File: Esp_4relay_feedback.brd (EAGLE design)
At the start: 100 x 100 mm, 58 parts, among them IC1 LM1117MP-3.3, IC2 7805TV, IC3 7805TV, IC4 7805TV, K1 G5LE, K2 G5LE, K3 G5LE, K4 G5LE, Q1 16MHz, SW1 Push Switch, T1 BC547, T2 BC547, T3 BC547, T4 BC547, U2 ATMEGA328P_PDIP

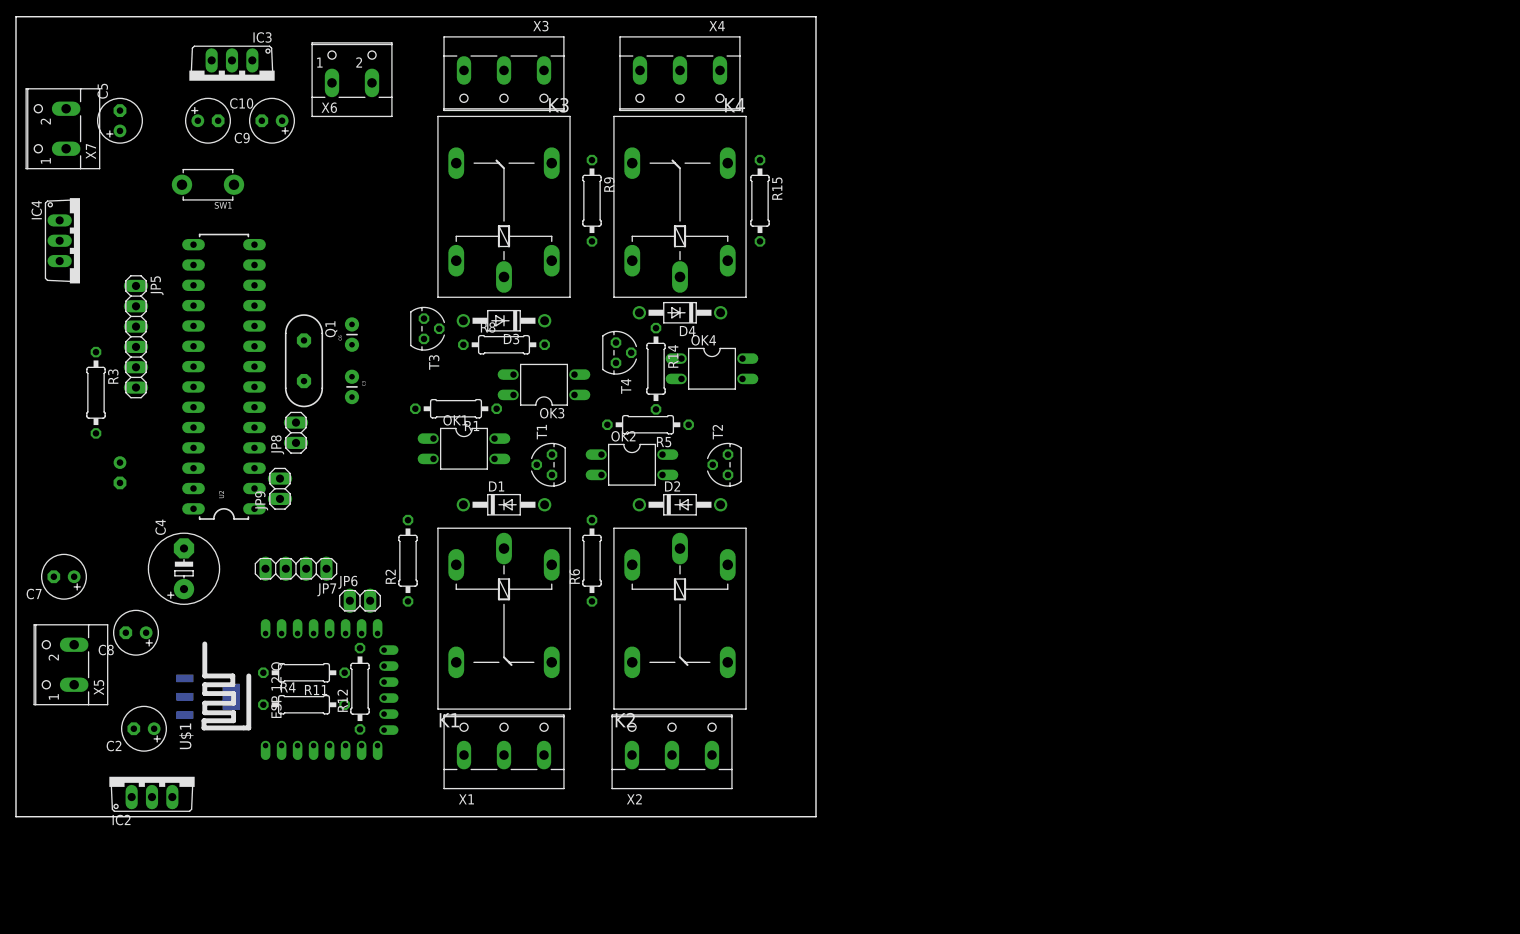
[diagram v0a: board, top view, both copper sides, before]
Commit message: added 8 relays
8 relays arranged in 4 up-down manner with
esp and atmega328 at left side.

routing 70% completed.
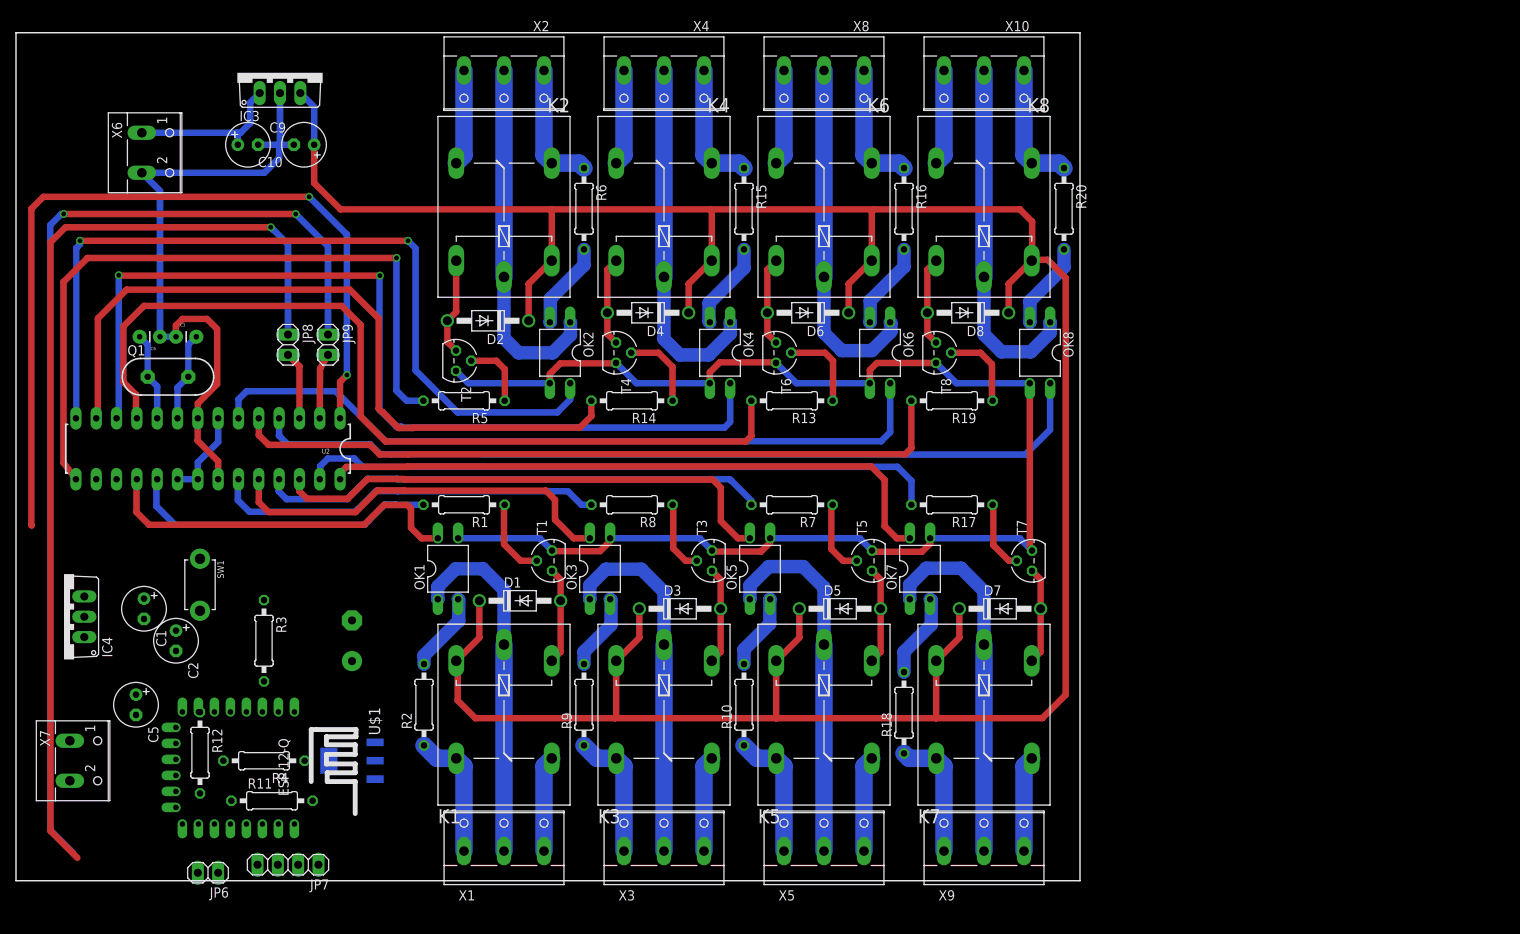
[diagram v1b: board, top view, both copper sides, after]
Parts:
- removed C7, C8: 10uf, rcl:E2,5-6
- removed IC2: 7805TV, linear:TO220V
- removed JP5: (no value), pinhead:1X06
- added D5, D6, D7, D8: 1N4007, diode:DO41-10
- added K5, K6, K7, K8: G5LE, relay:G5LE
- added OK5, OK6, OK7, OK8: PC817, optocoupler:DIL04
- added R10, R16, R18, R20: 220k, rcl:0207/10
- added R13, R17, R19, R7: 1k, rcl:0207/10
- added T5, T6, T7, T8: BC547, transistor:TO92
- added X10, X8, X9: (no value), con-wago-500:W237-103
- X5: device con-wago-500:W237-102 -> con-wago-500:W237-103
- moved X5 97.5 mm to (161.0, -3.00), turned to 0 degrees
- moved X3 97.1 mm to (141.0, -3.00), turned to 0 degrees
- moved X2 85.6 mm to (121.0, 92.0), turned to 180 degrees
- moved X7 79.1 mm to (68.0, 7.00), turned to 270 degrees
- moved C5 73.0 mm to (75.0, 14.0), turned to 270 degrees
- moved K3 68.0 mm to (141.0, 12.0), turned to 270 degrees
- moved R9 63.0 mm to (131.0, 14.0), turned to 90 degrees
- moved K2 57.4 mm to (121.0, 77.0), turned to 90 degrees
- moved SW1 50.0 mm to (83.0, 29.0), turned to 270 degrees
- moved IC4 47.0 mm to (66.0, 25.0), turned to 90 degrees
- moved T3 46.2 mm to (147.0, 32.0), turned to 90 degrees
- moved R6 44.0 mm to (131.0, 76.0), turned to 270 degrees
- moved D3 42.2 mm to (143.0, 26.0), turned to 0 degrees
- moved JP6 38.9 mm to (84.0, -7.00), turned to 180 degrees
- moved R3 37.4 mm to (91.0, 22.0)
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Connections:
- removed net ESP_SUPPLY: C2.+, C8.+, IC1.3, IC2.3
- new net F5: OK5.4, U2.26
- new net F6: OK6.4, U2.6
- new net F7: OK7.4, U2.28
- new net F8: OK8.4, U2.4
- new net N$34: OK5.2, R10.2
- new net N$35: R7.1, T5.2
- new net N$46: D5.A, K5.2, T5.3
- new net N$47: K6.P, OK6.1, X8.2
- new net N$48: K6.S, R16.1, X8.1
- new net N$49: OK6.2, R16.2
- new net N$50: R13.1, T6.2
- new net N$51: D6.A, K6.2, T6.3
- new net N$52: K7.P, OK7.1, X9.2
- new net N$53: K7.S, R18.1, X9.1
- new net N$54: OK7.2, R18.2
- new net N$55: R17.1, T7.2
- new net N$56: D7.A, K7.2, T7.3
- new net N$57: K8.P, OK8.1, X10.2
- new net N$58: K8.S, R20.1, X10.1
- new net N$59: OK8.2, R20.2
- new net N$60: R19.1, T8.2
- new net N$61: D8.A, K8.2, T8.3
- new net N$62: K5.O, X5.3
- new net N$63: K6.O, X8.3
- new net N$64: K7.O, X9.3
- new net N$65: K8.O, X10.3
- new net R5: R7.2, U2.25
- new net R6: R13.2, U2.11
- new net R7: R17.2, U2.27
- new net R8: R19.2, U2.5
- net F1: now also U2.18; no longer U2.5
- net F2: now also U2.14; no longer U2.11
- net F3: now also U2.24; no longer U2.13
- net F4: now also U2.12; no longer U2.15
- net GND: now also OK5.3, OK6.3, OK7.3, OK8.3, T5.1, T6.1, T7.1, T8.1; no longer C7.-, C8.-, IC2.2, JP5.6, X5.2
- net N$16: now also K5.P, OK5.1, X5.2; no longer JP5.3, U2.19
- net N$23: now also U2.16; no longer JP5.2, U2.18
- net N$26: now also U2.17; no longer C7.+, IC2.1, X5.1
- net N$32: now also K5.S, R10.1, X5.1; no longer JP5.1, U2.17
- net R1: now also U2.19; no longer U2.4
- net R2: now also U2.15; no longer U2.6
- net R3: now also U2.23; no longer U2.12
- net R4: now also U2.13; no longer U2.14
- net RELAY_SUPPLY: now also D5.C, D6.C, D7.C, D8.C, K5.1, K6.1, K7.1, K8.1
- net RESET: no longer JP5.4
- net VCC: now also C2.+, IC1.3; no longer JP5.5
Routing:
- net RELAY_SUPPLY: track 0.00 -> 353.8 mm
- net GND: track 0.00 -> 262.0 mm
- net TX1: track 0.00 -> 127.7 mm, vias 0 -> 2
- net RX1: track 0.00 -> 121.0 mm, vias 0 -> 1
- net F4: track 0.00 -> 117.3 mm, vias 0 -> 2
- net R6: track 0.00 -> 110.1 mm
- net F8: track 0.00 -> 106.7 mm
- net RESET: track 0.00 -> 105.0 mm, vias 0 -> 2
- net F2: track 0.00 -> 104.2 mm, vias 0 -> 2
- net F6: track 0.00 -> 93.4 mm
- net R4: track 0.00 -> 92.0 mm
- net R8: track 0.00 -> 90.9 mm
- net R2: track 0.00 -> 88.5 mm, vias 0 -> 1
- net R7: track 0.00 -> 80.1 mm
- net F7: track 0.00 -> 79.4 mm
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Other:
- board size 100 x 100 mm -> 133 x 106 mm

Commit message: routing done
board routing completed 100%
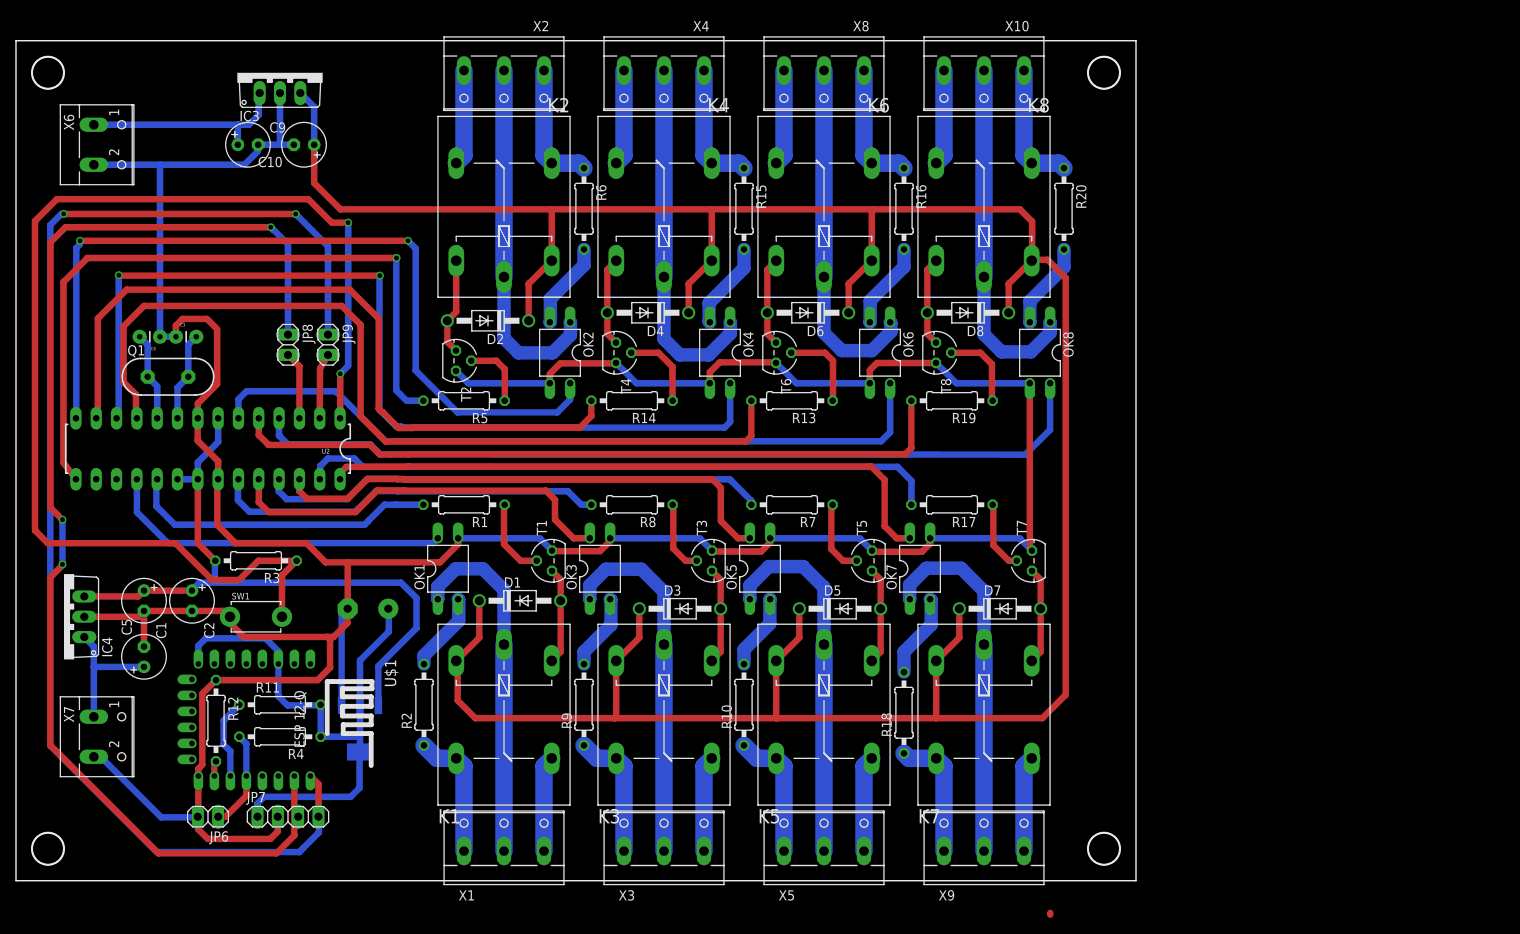
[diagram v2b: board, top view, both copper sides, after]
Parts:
- moved R11 12.0 mm to (93.0, 14.0)
- moved R3 10.0 mm to (90.0, 32.0), turned to 180 degrees
- moved SW1 8.06 mm to (90.0, 25.0), turned to 0 degrees
- moved JP6 7.00 mm to (84.0, 0.00)
- moved U$1 6.32 mm to (91.0, 12.0)
- moved C5 6.08 mm to (76.0, 20.0), turned to 90 degrees
- moved X6 6.08 mm to (71.0, 84.0)
- moved JP7 6.00 mm to (94.0, 0.00), turned to 0 degrees
- moved C2 5.39 mm to (82.0, 27.0)
- moved C4 4.47 mm to (104.0, 26.0), turned to 0 degrees
- moved R12 4.47 mm to (85.0, 12.0)
- moved X7 4.24 mm to (71.0, 10.0)
- moved IC1 4.12 mm to (103.0, 11.0), turned to 180 degrees
- moved R4 3.61 mm to (93.0, 10.0)
- moved C1 1.00 mm to (76.0, 27.0)
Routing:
- net GND: track 262.0 -> 431.3 mm
- net 3V3: track 0.00 -> 72.9 mm
- net VCC: track 11.2 -> 83.6 mm
- net RESET: track 105.0 -> 149.1 mm
- net TX1: track 127.7 -> 160.7 mm
- net RX1: track 121.0 -> 151.9 mm, vias 1 -> 3
- net N$33: track 0.00 -> 16.7 mm
- net IO0: track 0.00 -> 12.4 mm
- net N$21: track 0.00 -> 10.1 mm
- net N$27: track 19.8 -> 26.4 mm
- net F1: track 46.6 -> 43.6 mm
- net IO15: track 0.00 -> 1.90 mm
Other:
- board size 133 x 106 mm -> 140 x 105 mm

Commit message: component placing changed
Controller and esp placed in between relays.
routing done
PCB size : 130X95mm
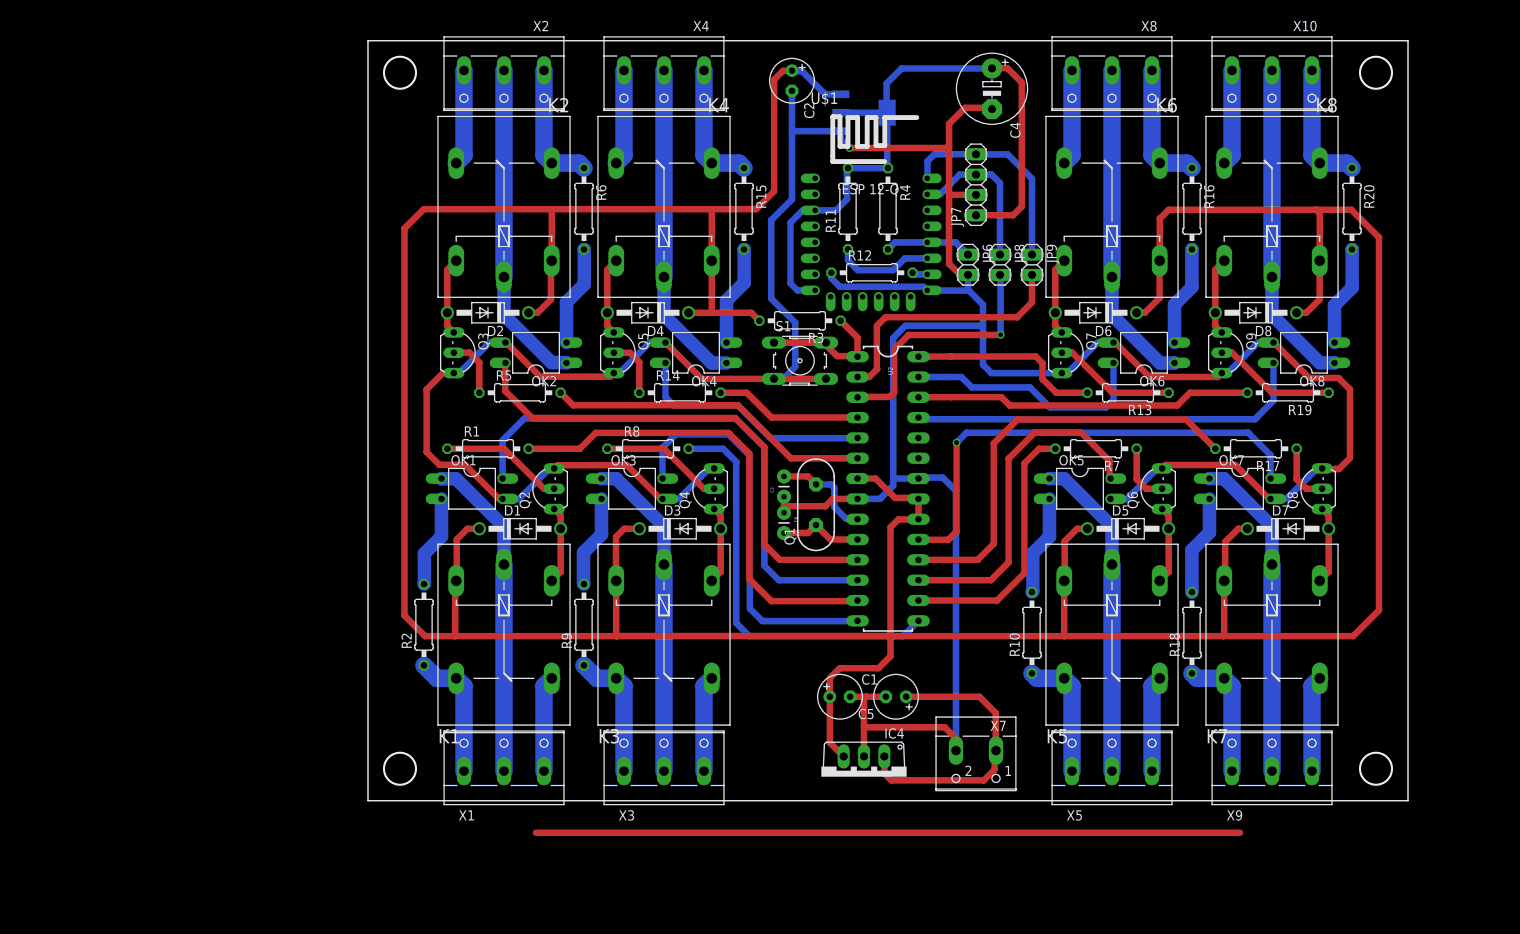
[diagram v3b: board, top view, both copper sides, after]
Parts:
- removed C10, C9: 10uf, rcl:E2,5-6
- removed IC3: 7805TV, linear:TO220V
- removed SW1: Push Switch, adafruit:TACT_PANA-EVQ
- removed T1, T2, T3, T4, T5, T6, T7, T8: BC547, transistor:TO92
- removed X6: (no value), con-wago-500:W237-102
- added Q2, Q3, Q4, Q5, Q6, Q7, Q8, Q9: BC547, transistor-npn:TO92-EBC
- added S1: (no value), switch-omron:B3F-10XX
- moved JP6 117.4 mm to (179.0, 69.0), turned to 270 degrees
- moved JP7 116.8 mm to (180.0, 79.0), turned to 90 degrees
- moved X7 109.0 mm to (180.0, 7.00), turned to 180 degrees
- moved IC4 102.0 mm to (166.0, 5.00), turned to 180 degrees
- moved C4 101.5 mm to (182.0, 91.0), flipped to the top, turned to 270 degrees
- moved R4 100.7 mm to (169.0, 76.0), turned to 270 degrees
- moved IC1 99.5 mm to (166.0, 88.0), turned to 90 degrees
- moved R12 99.3 mm to (167.0, 68.0), turned to 0 degrees
- moved C2 99.2 mm to (157.0, 92.0)
- moved U$1 98.1 mm to (167.0, 74.0), turned to 0 degrees
- moved R11 94.3 mm to (164.0, 76.0), turned to 90 degrees
- moved C5 94.1 mm to (170.0, 15.0), turned to 180 degrees
- moved JP8 89.6 mm to (183.0, 69.0)
- moved JP9 88.6 mm to (187.0, 69.0)
- moved C1 87.8 mm to (163.0, 15.0), turned to 0 degrees
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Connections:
- removed net N$23: U2.16
- removed net N$26: U2.17
- removed net N$27: C9.+, IC3.1, X6.1
- removed net RELAY_SUPPLY: C10.+, D1.C, D2.C, D3.C, D4.C, D5.C, D6.C, D7.C, D8.C, IC3.3, K1.1, K2.1, K3.1, K4.1, K5.1, K6.1, K7.1, K8.1
- new net ERT: U2.23
- new net WE: U2.24
- net F1: now also U2.12; no longer U2.18
- net F2: now also U2.11; no longer U2.14
- net F3: now also U2.14; no longer U2.24
- net F4: now also U2.5; no longer U2.12
- net F5: now also U2.17; no longer U2.26
- net F6: now also U2.27; no longer U2.6
- net F7: now also U2.19; no longer U2.28
- net F8: now also U2.25; no longer U2.4
- net GND: now also Q2.E, Q3.E, Q4.E, Q5.E, Q6.E, Q7.E, Q8.E, Q9.E, S1.3, S1.4; no longer C10.-, C9.-, IC3.2, SW1.P$1, T1.1, T2.1, T3.1, T4.1, T5.1, T6.1, T7.1, T8.1, X6.2
- net N$11: now also Q3.B; no longer T2.2
- net N$12: now also Q3.C; no longer T2.3
- net N$17: now also Q4.B; no longer T3.2
- net N$18: now also Q4.C; no longer T3.3
- net N$24: now also Q5.B; no longer T4.2
- net N$25: now also Q5.C; no longer T4.3
- net N$35: now also Q6.B; no longer T5.2
- net N$46: now also Q6.C; no longer T5.3
- net N$50: now also Q7.B; no longer T6.2
- net N$51: now also Q7.C; no longer T6.3
- net N$55: now also Q8.B; no longer T7.2
- net N$56: now also Q8.C; no longer T7.3
- net N$60: now also Q9.B; no longer T8.2
- net N$61: now also Q9.C; no longer T8.3
- net N$7: now also Q2.B; no longer T1.2
- net N$8: now also Q2.C; no longer T1.3
- net R1: now also U2.13; no longer U2.19
- net R2: now also U2.6; no longer U2.15
- net R3: now also U2.15; no longer U2.23
- net R4: now also U2.4; no longer U2.13
- net R5: now also U2.16; no longer U2.25
- net R6: now also U2.28; no longer U2.11
- net R7: now also U2.18; no longer U2.27
- net R8: now also U2.26; no longer U2.5
- net RESET: now also S1.1, S1.2; no longer SW1.P$2
- net VCC: now also D1.C, D2.C, D3.C, D4.C, D5.C, D6.C, D7.C, D8.C, K1.1, K2.1, K3.1, K4.1, K5.1, K6.1, K7.1, K8.1
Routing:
- net VCC: track 83.6 -> 499.1 mm
- net RELAY_SUPPLY: track 353.8 -> 0.00 mm
- net TX1: track 160.7 -> 26.3 mm, vias 2 -> 0
- net RX1: track 151.9 -> 19.5 mm, vias 3 -> 0
- net RESET: track 149.1 -> 16.7 mm, vias 2 -> 0
- net N$23: track 0.00 -> 88.0 mm
- net F4: track 117.3 -> 30.4 mm, vias 2 -> 0
- net R6: track 110.1 -> 24.1 mm
- net R4: track 92.0 -> 18.4 mm
- net F6: track 93.4 -> 31.0 mm
- net F8: track 106.7 -> 50.2 mm
- net R8: track 90.9 -> 42.2 mm
- net R2: track 88.5 -> 40.5 mm, vias 1 -> 0
- net F2: track 104.2 -> 63.4 mm, vias 2 -> 0
- net R5: track 63.7 -> 33.0 mm
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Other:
- board size 140 x 105 mm -> 130 x 95 mm
